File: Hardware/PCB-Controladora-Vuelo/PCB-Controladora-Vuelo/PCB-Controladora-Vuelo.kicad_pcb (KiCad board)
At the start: 2 copper layers, 40 x 90 mm, 14 parts, among them J1 Jumper Serial, J2 CONN, U1 MPU-5060, U2 ESP32-DEVKIT-V1, U3 Nrf24l01, U4 AMS1117-3.3

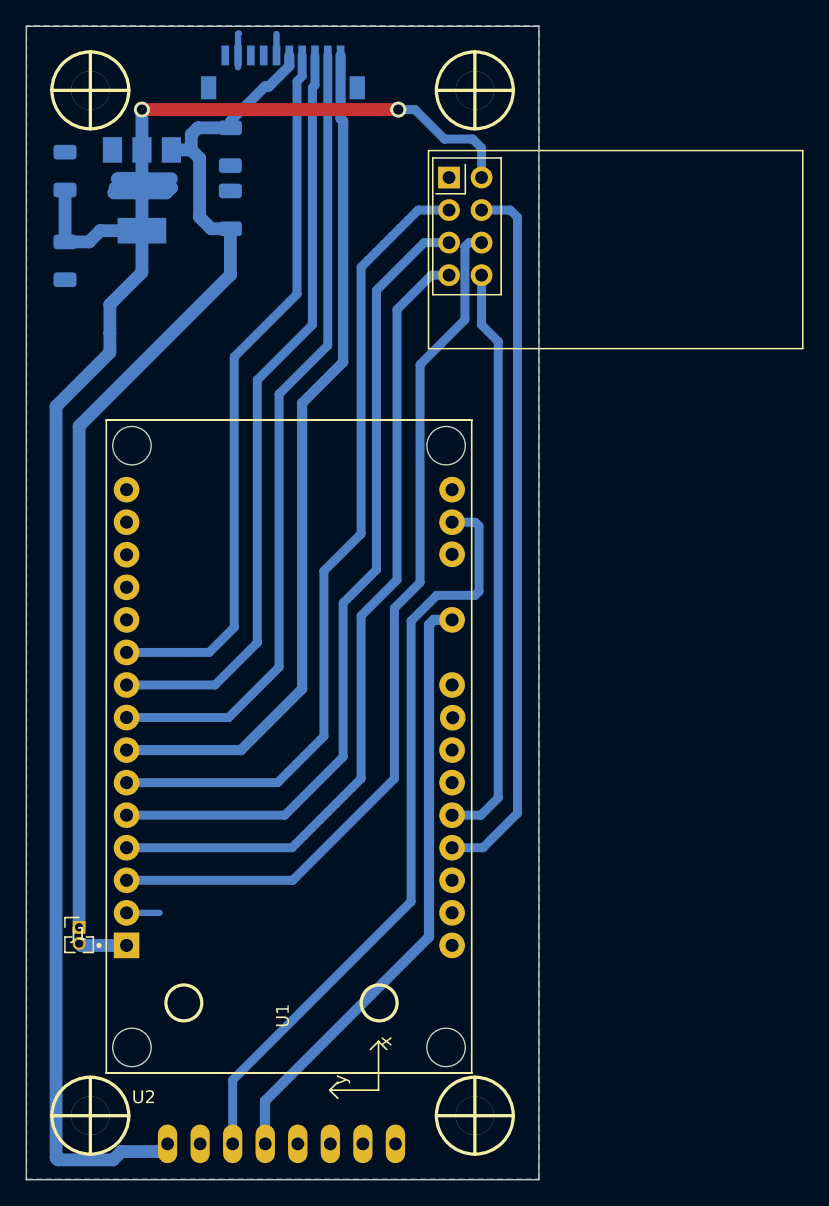
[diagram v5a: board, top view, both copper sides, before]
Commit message: MODIFIQUE ESQUEMATICO Y PCB FINALIZADO DIRIA yo falta aprobacion de legui lo deje con 2 puentes para mas seguridad , nuevo puente pin MOSI NRF24L01 Y PLACA LISTA CHEQUEO EL 3D Y VAVVAVVAVA
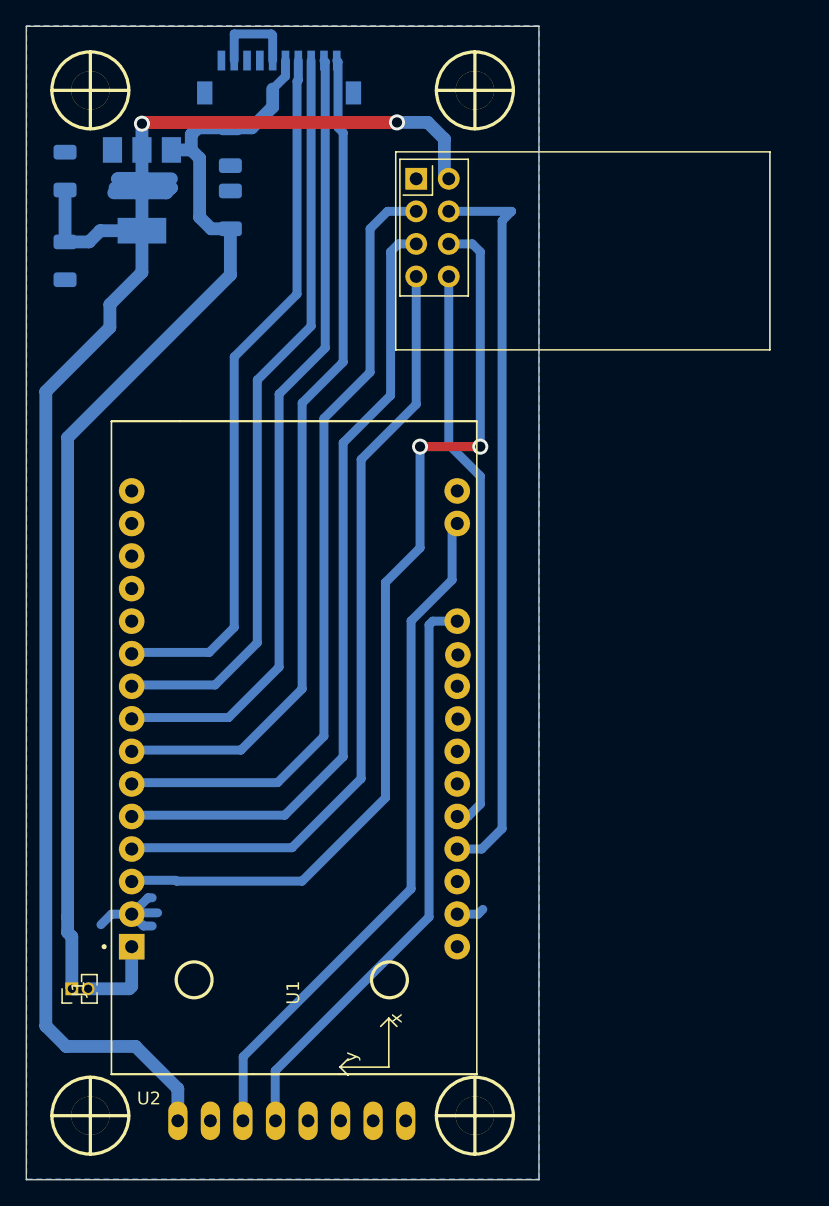
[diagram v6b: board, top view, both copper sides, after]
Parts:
- moved J1 4.83 mm to (117.5, 125.9), turned to 90 degrees
- moved U3 2.56 mm to (144.4, 62.7)
- moved U1 1.97 mm to (125.8, 136.2)
- moved J2 0.50 mm to (133.7, 56.0)
- moved U2 0.41 mm to (134.4, 107.1)
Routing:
- net GND: track 6.92 -> 18.2 mm
- net +3V3: track 149.5 -> 141.5 mm
- net /SCL_MPU6050: track 60.1 -> 53.5 mm
- net +5V: track 81.4 -> 87.0 mm
- net /MOSI_NRF24L01: track 69.4 -> 73.7 mm, vias 0 -> 2
- net /Jumper_Serial: track 3.76 -> 6.70 mm
- net /MISO_NRF24L01: track 63.5 -> 61.1 mm
- net /SCK_NRF24L01: track 63.5 -> 61.6 mm
- net /CSN_NRF24L01: track 55.7 -> 57.5 mm
- net /SDA_MPU6050: track 47.8 -> 46.0 mm
- net /CE_NRF24L01: track 63.4 -> 61.8 mm
- net /IRQ_NRF24L01: track 45.5 -> 44.4 mm
- net /S1_MOTOR: track 56.0 -> 55.1 mm
- net /S2_MOTOR: track 59.3 -> 58.4 mm
- net /S3_MOTOR: track 62.8 -> 62.0 mm
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
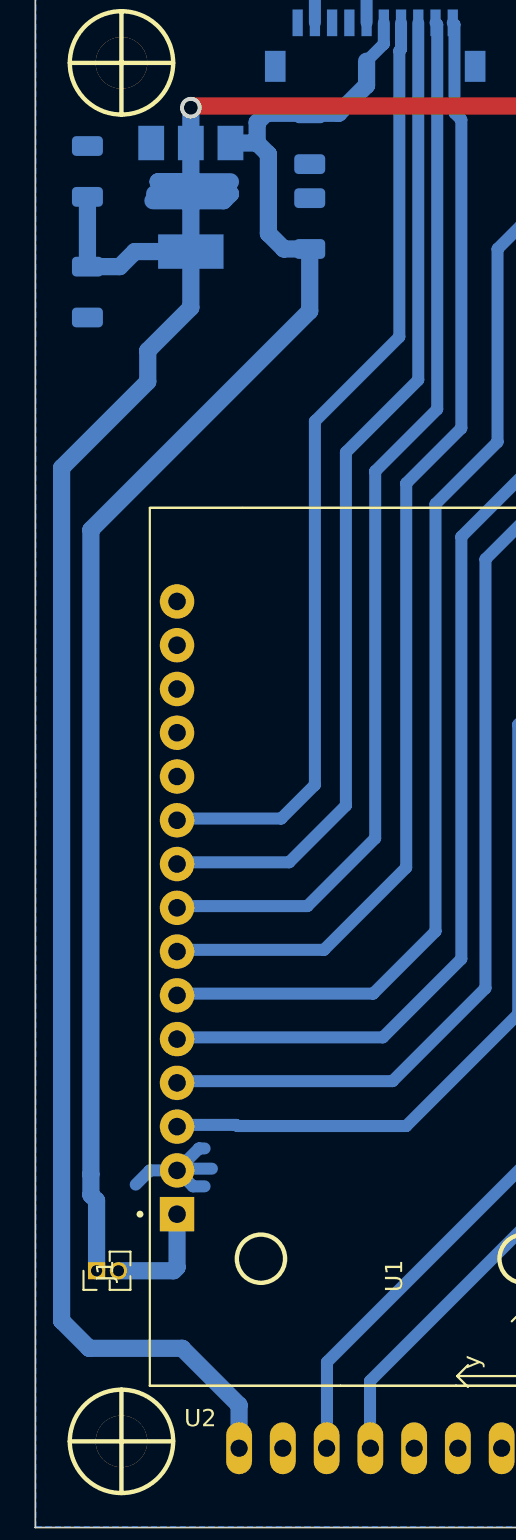
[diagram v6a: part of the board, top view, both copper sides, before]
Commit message: Cambie capacitores y agregue componentes smd , quedo bien cambie los capacitores electroliticos , queda duda de la huella jst y el posicionamiento de los agujeros de sujecion y ajustar la placa a un tamaño comodo
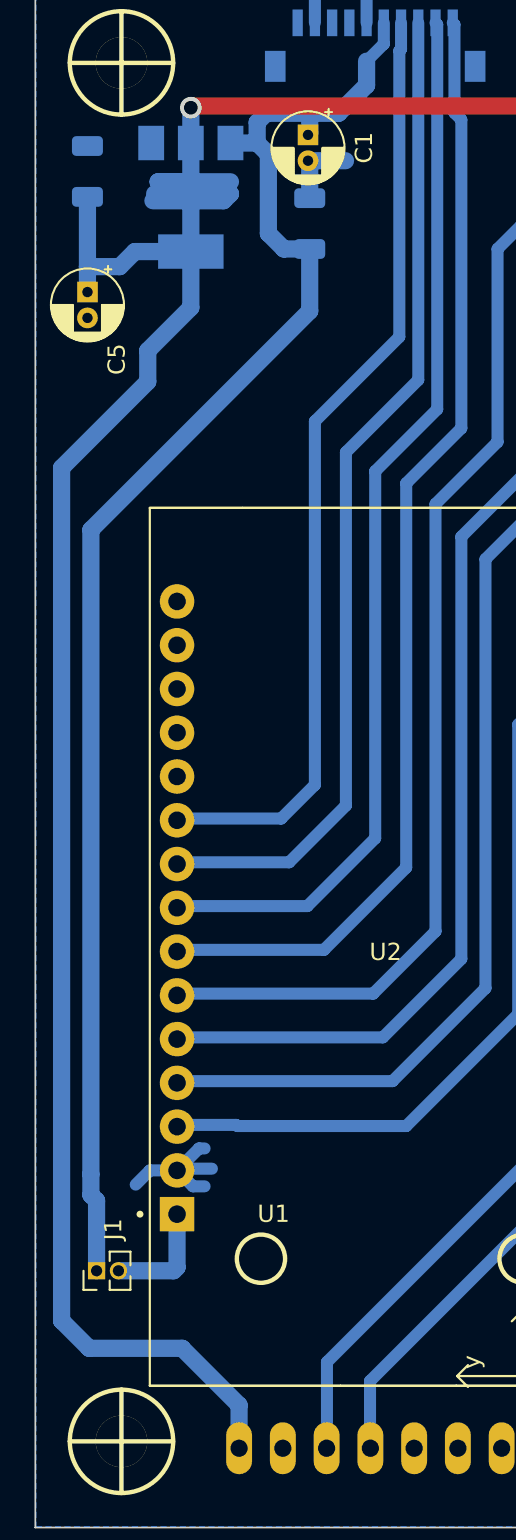
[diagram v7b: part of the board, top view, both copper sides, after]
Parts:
- C1, C5: footprint Capacitor_SMD:C_1206_3216Metric -> Capacitor_THT:CP_Radial_D4.0mm_P1.50mm; moved to F.Cu
- J2: value CONN -> ESC
- U1: value MPU-5060 -> MPU-6050
- moved C1 0.24 mm to (129.8, 60.0)
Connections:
- U2 pad 21: (no net) -> unconnected-(U2-D19-Pad21)
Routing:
- net GND: track 18.2 -> 22.6 mm
- net +3V3: track 141.5 -> 143.0 mm
- net +5V: track 87.0 -> 88.3 mm
